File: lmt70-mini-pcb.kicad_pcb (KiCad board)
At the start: 4 copper layers, 7.8 x 8.4 mm, 3 parts, among them P1 CONN_01X04, U1 LMT70

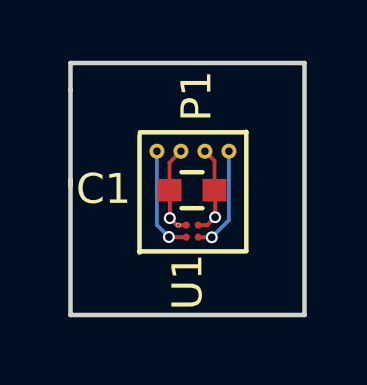
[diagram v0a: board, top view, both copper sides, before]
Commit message: updated pcb to fit bigger cables
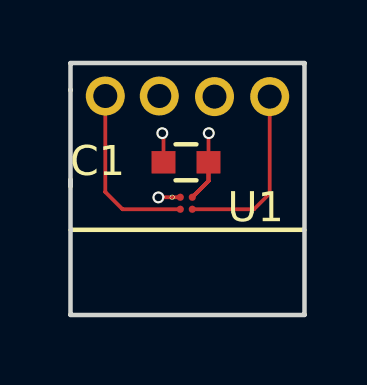
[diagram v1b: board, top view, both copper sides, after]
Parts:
- moved P1 1.94 mm to (150.5, 105.9)
- moved C1 0.95 mm to (151.8, 108.2)
- moved U1 0.95 mm to (151.7, 109.4)
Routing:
- net Net-(P1-Pad4): track 3.56 -> 6.03 mm, vias 1 -> 0
- net Net-(P1-Pad1): track 3.61 -> 5.94 mm, vias 1 -> 0
- net Net-(C1-Pad2): track 5.42 -> 6.46 mm, vias 1 -> 2
- added copper zone on In2.Cu, net Net-(C1-Pad1)
- added copper zone on In1.Cu, net Net-(C1-Pad2)
- removed copper zone on In1.Cu, net Net-(C1-Pad1)
- removed copper zone on In2.Cu, net Net-(C1-Pad2)
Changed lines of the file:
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@@
     (links 6)
     (no_connects 0)
-    (area 146.539667 104.824999 156.460334 113.375001)
+    (area 146.169667 102.996809 156.290001 113.375001)
     (thickness 1.6)
-    (drawings 10)
-    (tracks 28)
+    (drawings 7)
+    (tracks 26)
     (zones 0)
     (modules 3)
@@
     (mod_text_size 1 1)
     (mod_text_width 0.15)
-    (pad_size 1.524 1.524)
-    (pad_drill 0.762)
+    (pad_size 1.3 1.3)
+    (pad_drill 0.8)
     (pad_to_mask_clearance 0.0635)
     (aux_axis_origin 0 0)
@@
   )
   (module Capacitors_SMD:C_0603 (layer F.Cu)
-    (at 152.05 109.14 180)
+    (at 151.85 108.21 180)
     (descr "Capacitor SMD 0603, reflow soldering, AVX (see smccp.pdf)")
     (tags "capacitor 0603")
@@
   )
   (module lmt70:Wire_1x04_mini (layer F.Cu)
-    (at 150.88 107.84)
-    (fp_text reference P1 (at 1.32 -1.84 90) (layer F.SilkS)
+    (at 150.51 105.94)
+    (fp_text reference P1 (at 1.32 -1.84 90) (layer F.SilkS) hide
       (effects (font (size 1 1) (thickness 0.15)))
     )
@@
       (effects (font (size 1 1) (thickness 0.15)))
     )
-    (pad 1 thru_hole circle (at 0 0) (size 0.5 0.5) (drill 0.254) (layers *.Cu *.Mask)
+    (pad 1 thru_hole circle (at -1.35 0.06) (size 1.3 1.3) (drill 0.8) (layers *.Cu *.Mask)
       (net 3 "Net-(P1-Pad1)"))
-    (pad 2 thru_hole circle (at 0.8 0) (size 0.5 0.5) (drill 0.254) (layers *.Cu *.Mask)
+    (pad 2 thru_hole circle (at 0.45 0.06) (size 1.3 1.3) (drill 0.8) (layers *.Cu *.Mask)
       (net 2 "Net-(C1-Pad2)"))
-    (pad 3 thru_hole circle (at 1.6 0) (size 0.5 0.5) (drill 0.254) (layers *.Cu *.Mask)
+    (pad 3 thru_hole circle (at 2.29 0.08) (size 1.3 1.3) (drill 0.8) (layers *.Cu *.Mask)
       (net 1 "Net-(C1-Pad1)"))
-    (pad 4 thru_hole circle (at 2.4 0) (size 0.5 0.5) (drill 0.254) (layers *.Cu *.Mask)
+    (pad 4 thru_hole circle (at 4.13 0.08) (size 1.3 1.3) (drill 0.8) (layers *.Cu *.Mask)
       (net 4 "Net-(P1-Pad4)"))
   )
   (module lmt70:LMT70 (layer F.Cu)
-    (at 151.859524 110.305)
-    (fp_text reference U1 (at 0.040476 1.895 90) (layer F.SilkS)
+    (at 151.659524 109.375)
+    (fp_text reference U1 (at 2.510476 0.335 180) (layer F.SilkS)
       (effects (font (size 1 1) (thickness 0.15)))
     )
@@
   (gr_line (start 148 105.8) (end 148 104.9) (angle 90) (layer Edge.Cuts) (width 0.15))
   (gr_line (start 148 109) (end 148 105.8) (angle 90) (layer Edge.Cuts) (width 0.15))
-  (gr_line (start 153.86 107.21) (end 150.31 107.21) (angle 90) (layer F.SilkS) (width 0.15))
-  (gr_line (start 153.86 111.16) (end 153.86 107.19) (angle 90) (layer F.SilkS) (width 0.15))
-  (gr_line (start 150.3 111.18) (end 153.86 111.18) (angle 90) (layer F.SilkS) (width 0.15))
-  (gr_line (start 150.3 107.31) (end 150.3 111.22) (angle 90) (layer F.SilkS) (width 0.15))
-  (segment (start 152.8 109.14) (end 152.8 108.16) (width 0.127) (layer F.Cu) (net 1))
-  (segment (start 152.8 108.16) (end 152.48 107.84) (width 0.127) (layer F.Cu) (net 1))
-  (segment (start 152.82 110.04) (end 152.82 109.16) (width 0.127) (layer F.Cu) (net 1))
-  (segment (start 152.82 109.16) (end 152.8 109.14) (width 0.127) (layer F.Cu) (net 1))
-  (segment (start 152.555 110.305) (end 152.259524 110.305) (width 0.127) (layer F.Cu) (net 1))
-  (segment (start 152.82 110.04) (end 152.555 110.305) (width 0.127) (layer F.Cu) (net 1))
-  (via (at 152.82 110.04) (size 0.4) (drill 0.254) (layers F.Cu B.Cu) (net 1))
-  (segment (start 152.48 107.84) (end 152.48 109.7) (width 0.127) (layer In2.Cu) (net 1))
-  (segment (start 152.48 109.7) (end 152.82 110.04) (width 0.127) (layer In2.Cu) (net 1))
-  (segment (start 151.31 110.07) (end 151.31 109.15) (width 0.127) (layer F.Cu) (net 2))
-  (segment (start 151.31 109.15) (end 151.3 109.14) (width 0.127) (layer F.Cu) (net 2))
-  (segment (start 151.3 109.14) (end 151.3 108.22) (width 0.127) (layer F.Cu) (net 2))
-  (segment (start 151.3 108.22) (end 151.68 107.84) (width 0.127) (layer F.Cu) (net 2))
-  (segment (start 151.859524 110.305) (end 151.545 110.305) (width 0.127) (layer F.Cu) (net 2))
-  (segment (start 151.68 109.7) (end 151.68 107.84) (width 0.127) (layer In1.Cu) (net 2))
-  (segment (start 151.31 110.07) (end 151.68 109.7) (width 0.127) (layer In1.Cu) (net 2))
-  (via (at 151.31 110.07) (size 0.4) (drill 0.254) (layers F.Cu B.Cu) (net 2))
-  (segment (start 151.545 110.305) (end 151.31 110.07) (width 0.127) (layer F.Cu) (net 2))
-  (segment (start 150.88 110.3) (end 150.88 107.84) (width 0.127) (layer B.Cu) (net 3))
-  (segment (start 151.28 110.7) (end 150.88 110.3) (width 0.127) (layer B.Cu) (net 3))
-  (via (at 151.28 110.7) (size 0.4) (drill 0.254) (layers F.Cu B.Cu) (net 3))
-  (segment (start 151.285 110.705) (end 151.28 110.7) (width 0.127) (layer F.Cu) (net 3))
-  (segment (start 151.859524 110.705) (end 151.285 110.705) (width 0.127) (layer F.Cu) (net 3))
-  (segment (start 152.259524 110.705) (end 152.705 110.705) (width 0.127) (layer F.Cu) (net 4))
-  (segment (start 153.28 110.14) (end 153.28 107.84) (width 0.127) (layer B.Cu) (net 4))
-  (segment (start 152.71 110.71) (end 153.28 110.14) (width 0.127) (layer B.Cu) (net 4))
-  (via (at 152.71 110.71) (size 0.4) (drill 0.254) (layers F.Cu B.Cu) (net 4))
-  (segment (start 152.705 110.705) (end 152.71 110.71) (width 0.127) (layer F.Cu) (net 4))
-  (zone (net 1) (net_name "Net-(C1-Pad1)") (layer In1.Cu) (hatch edge 0.508)
+  (gr_line (start 148 110.46) (end 155.8 110.46) (angle 90) (layer F.SilkS) (width 0.15))
+  (segment (start 152.6 108.21) (end 152.6 108.834524) (width 0.127) (layer F.Cu) (net 1))
+  (segment (start 152.6 108.834524) (end 152.059524 109.375) (width 0.127) (layer F.Cu) (net 1))
+  (segment (start 152.8 106.02) (end 152.8 107.05) (width 0.127) (layer In2.Cu) (net 1))
+  (segment (start 152.8 107.05) (end 152.61 107.24) (width 0.127) (layer In2.Cu) (net 1))
+  (via (at 152.61 107.24) (size 0.4) (drill 0.254) (layers F.Cu B.Cu) (net 1))
+  (segment (start 152.61 107.24) (end 152.6 107.25) (width 0.127) (layer F.Cu) (net 1))
+  (segment (start 152.6 107.25) (end 152.6 108.834524) (width 0.127) (layer F.Cu) (net 1))
+  (segment (start 152.6 108.834524) (end 152.059524 109.375) (width 0.127) (layer F.Cu) (net 1))
+  (segment (start 152.62 108.23) (end 152.6 108.21) (width 0.127) (layer F.Cu) (net 1))
+  (segment (start 151.659524 109.375) (end 150.935 109.375) (width 0.127) (layer F.Cu) (net 2))
+  (segment (start 150.79 109.24) (end 150.96 106) (width 0.127) (layer In1.Cu) (net 2))
+  (segment (start 150.93 109.38) (end 150.79 109.24) (width 0.127) (layer In1.Cu) (net 2))
+  (via (at 150.93 109.38) (size 0.4) (drill 0.254) (layers F.Cu B.Cu) (net 2))
+  (segment (start 150.935 109.375) (end 150.93 109.38) (width 0.127) (layer F.Cu) (net 2))
+  (segment (start 150.96 106) (end 150.96 107.14) (width 0.127) (layer In1.Cu) (net 2))
+  (segment (start 151.1 107.28) (end 151.1 108.21) (width 0.127) (layer F.Cu) (net 2))
+  (segment (start 151.06 107.24) (end 151.1 107.28) (width 0.127) (layer F.Cu) (net 2))
+  (via (at 151.06 107.24) (size 0.4) (drill 0.254) (layers F.Cu B.Cu) (net 2))
+  (segment (start 150.96 107.14) (end 151.06 107.24) (width 0.127) (layer In1.Cu) (net 2))
+  (segment (start 151.11 108.22) (end 151.1 108.21) (width 0.127) (layer F.Cu) (net 2))
+  (segment (start 151.659524 109.775) (end 149.735 109.775) (width 0.127) (layer F.Cu) (net 3))
+  (segment (start 149.16 109.2) (end 149.16 106) (width 0.127) (layer F.Cu) (net 3))
+  (segment (start 149.735 109.775) (end 149.16 109.2) (width 0.127) (layer F.Cu) (net 3))
+  (segment (start 152.059524 109.775) (end 154.115 109.775) (width 0.127) (layer F.Cu) (net 4))
+  (segment (start 154.64 109.25) (end 154.64 106.02) (width 0.127) (layer F.Cu) (net 4))
+  (segment (start 154.115 109.775) (end 154.64 109.25) (width 0.127) (layer F.Cu) (net 4))
+  (zone (net 1) (net_name "Net-(C1-Pad1)") (layer In2.Cu) (hatch edge 0.508)
     (connect_pads (clearance 0.127))
     (min_thickness 0.127)
@@
     (polygon
       (pts
-        (xy 153.9 111.2) (xy 150.35 111.28) (xy 150.37 107.2) (xy 153.98 107.13)
+        (xy 155.86 104.83) (xy 155.859964 104.84) (xy 155.86 104.84) (xy 155.85 110.38) (xy 155.840036 110.38)
+        (xy 155.84 110.39) (xy 147.97 110.39) (xy 147.969982 110.38) (xy 147.95 110.38) (xy 147.92 104.82)
+        (xy 147.96 104.820101) (xy 147.96 104.82)
       )
     )
   )
-  (zone (net 2) (net_name "Net-(C1-Pad2)") (layer In2.Cu) (hatch edge 0.508)
+  (zone (net 2) (net_name "Net-(C1-Pad2)") (layer In1.Cu) (hatch edge 0.508)
     (connect_pads (clearance 0.127))
     (min_thickness 0.127)
@@
     (polygon
       (pts
-        (xy 153.94 111.27) (xy 150.27 111.27) (xy 150.27 107.246233) (xy 153.91 107.06)
+        (xy 147.72 104.49) (xy 147.69 110.47) (xy 156.29 110.46) (xy 156.29 104.58)
       )
     )

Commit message: termo buffer from cable
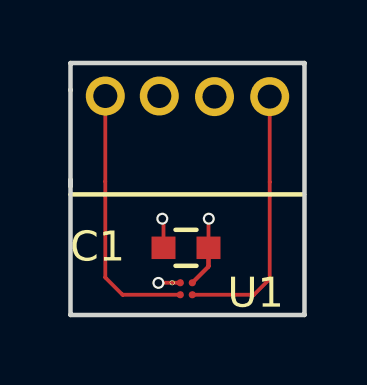
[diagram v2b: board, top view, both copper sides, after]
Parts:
- moved C1 2.85 mm to (151.8, 111.1)
- moved U1 2.85 mm to (151.7, 112.2)
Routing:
- net Net-(C1-Pad2): track 6.46 -> 9.37 mm
- net Net-(P1-Pad4): track 6.03 -> 8.88 mm
- net Net-(P1-Pad1): track 5.94 -> 8.79 mm
- net Net-(C1-Pad1): track 5.08 -> 7.93 mm
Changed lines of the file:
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@@
     (thickness 1.6)
     (drawings 7)
-    (tracks 26)
+    (tracks 32)
     (zones 0)
     (modules 3)
@@
   )
   (module Capacitors_SMD:C_0603 (layer F.Cu)
-    (at 151.85 108.21 180)
+    (at 151.85 111.06 180)
     (descr "Capacitor SMD 0603, reflow soldering, AVX (see smccp.pdf)")
     (tags "capacitor 0603")
@@
   )
   (module lmt70:LMT70 (layer F.Cu)
-    (at 151.659524 109.375)
+    (at 151.659524 112.225)
     (fp_text reference U1 (at 2.510476 0.335 180) (layer F.SilkS)
       (effects (font (size 1 1) (thickness 0.15)))
@@
   (gr_line (start 148 105.8) (end 148 104.9) (angle 90) (layer Edge.Cuts) (width 0.15))
   (gr_line (start 148 109) (end 148 105.8) (angle 90) (layer Edge.Cuts) (width 0.15))
-  (gr_line (start 148 110.46) (end 155.8 110.46) (angle 90) (layer F.SilkS) (width 0.15))
-  (segment (start 152.6 108.21) (end 152.6 108.834524) (width 0.127) (layer F.Cu) (net 1))
-  (segment (start 152.6 108.834524) (end 152.059524 109.375) (width 0.127) (layer F.Cu) (net 1))
-  (segment (start 152.8 106.02) (end 152.8 107.05) (width 0.127) (layer In2.Cu) (net 1))
-  (segment (start 152.8 107.05) (end 152.61 107.24) (width 0.127) (layer In2.Cu) (net 1))
-  (via (at 152.61 107.24) (size 0.4) (drill 0.254) (layers F.Cu B.Cu) (net 1))
-  (segment (start 152.61 107.24) (end 152.6 107.25) (width 0.127) (layer F.Cu) (net 1))
-  (segment (start 152.6 107.25) (end 152.6 108.834524) (width 0.127) (layer F.Cu) (net 1))
-  (segment (start 152.6 108.834524) (end 152.059524 109.375) (width 0.127) (layer F.Cu) (net 1))
-  (segment (start 152.62 108.23) (end 152.6 108.21) (width 0.127) (layer F.Cu) (net 1))
-  (segment (start 151.659524 109.375) (end 150.935 109.375) (width 0.127) (layer F.Cu) (net 2))
-  (segment (start 150.79 109.24) (end 150.96 106) (width 0.127) (layer In1.Cu) (net 2))
-  (segment (start 150.93 109.38) (end 150.79 109.24) (width 0.127) (layer In1.Cu) (net 2))
-  (via (at 150.93 109.38) (size 0.4) (drill 0.254) (layers F.Cu B.Cu) (net 2))
-  (segment (start 150.935 109.375) (end 150.93 109.38) (width 0.127) (layer F.Cu) (net 2))
-  (segment (start 150.96 106) (end 150.96 107.14) (width 0.127) (layer In1.Cu) (net 2))
-  (segment (start 151.1 107.28) (end 151.1 108.21) (width 0.127) (layer F.Cu) (net 2))
-  (segment (start 151.06 107.24) (end 151.1 107.28) (width 0.127) (layer F.Cu) (net 2))
-  (via (at 151.06 107.24) (size 0.4) (drill 0.254) (layers F.Cu B.Cu) (net 2))
-  (segment (start 150.96 107.14) (end 151.06 107.24) (width 0.127) (layer In1.Cu) (net 2))
-  (segment (start 151.11 108.22) (end 151.1 108.21) (width 0.127) (layer F.Cu) (net 2))
-  (segment (start 151.659524 109.775) (end 149.735 109.775) (width 0.127) (layer F.Cu) (net 3))
-  (segment (start 149.16 109.2) (end 149.16 106) (width 0.127) (layer F.Cu) (net 3))
-  (segment (start 149.735 109.775) (end 149.16 109.2) (width 0.127) (layer F.Cu) (net 3))
-  (segment (start 152.059524 109.775) (end 154.115 109.775) (width 0.127) (layer F.Cu) (net 4))
-  (segment (start 154.64 109.25) (end 154.64 106.02) (width 0.127) (layer F.Cu) (net 4))
-  (segment (start 154.115 109.775) (end 154.64 109.25) (width 0.127) (layer F.Cu) (net 4))
+  (gr_line (start 147.99 109.28) (end 155.79 109.28) (angle 90) (layer F.SilkS) (width 0.15))
+  (segment (start 152.8 106.02) (end 152.8 108.87) (width 0.127) (layer In2.Cu) (net 1))
+  (segment (start 152.6 110.1) (end 152.6 111.684524) (width 0.127) (layer F.Cu) (net 1))
+  (segment (start 152.61 110.09) (end 152.6 110.1) (width 0.127) (layer F.Cu) (net 1))
+  (via (at 152.61 110.09) (size 0.4) (drill 0.254) (layers F.Cu B.Cu) (net 1))
+  (segment (start 152.8 109.9) (end 152.61 110.09) (width 0.127) (layer In2.Cu) (net 1))
+  (segment (start 152.8 108.87) (end 152.8 109.9) (width 0.127) (layer In2.Cu) (net 1))
+  (segment (start 152.6 111.06) (end 152.6 111.684524) (width 0.127) (layer F.Cu) (net 1))
+  (segment (start 152.6 111.684524) (end 152.059524 112.225) (width 0.127) (layer F.Cu) (net 1))
+  (segment (start 152.6 111.684524) (end 152.059524 112.225) (width 0.127) (layer F.Cu) (net 1))
+  (segment (start 152.62 111.08) (end 152.6 111.06) (width 0.127) (layer F.Cu) (net 1))
+  (segment (start 150.956833 108.910359) (end 150.956833 106.003167) (width 0.127) (layer In1.Cu) (net 2))
+  (segment (start 150.956833 106.003167) (end 150.96 106) (width 0.127) (layer In1.Cu) (net 2))
+  (segment (start 151.659524 112.225) (end 150.935 112.225) (width 0.127) (layer F.Cu) (net 2))
+  (segment (start 150.79 112.09) (end 150.956833 108.910359) (width 0.127) (layer In1.Cu) (net 2))
+  (segment (start 150.956833 108.910359) (end 150.96 108.85) (width 0.127) (layer In1.Cu) (net 2))
+  (segment (start 150.93 112.23) (end 150.79 112.09) (width 0.127) (layer In1.Cu) (net 2))
+  (via (at 150.93 112.23) (size 0.4) (drill 0.254) (layers F.Cu B.Cu) (net 2))
+  (segment (start 150.935 112.225) (end 150.93 112.23) (width 0.127) (layer F.Cu) (net 2))
+  (segment (start 150.96 108.85) (end 150.96 109.99) (width 0.127) (layer In1.Cu) (net 2))
+  (segment (start 151.1 110.13) (end 151.1 111.06) (width 0.127) (layer F.Cu) (net 2))
+  (segment (start 151.06 110.09) (end 151.1 110.13) (width 0.127) (layer F.Cu) (net 2))
+  (via (at 151.06 110.09) (size 0.4) (drill 0.254) (layers F.Cu B.Cu) (net 2))
+  (segment (start 150.96 109.99) (end 151.06 110.09) (width 0.127) (layer In1.Cu) (net 2))
+  (segment (start 151.11 111.07) (end 151.1 111.06) (width 0.127) (layer F.Cu) (net 2))
+  (segment (start 149.16 106) (end 149.16 108.85) (width 0.127) (layer F.Cu) (net 3))
+  (segment (start 149.735 112.625) (end 149.16 112.05) (width 0.127) (layer F.Cu) (net 3))
+  (segment (start 149.16 112.05) (end 149.16 108.85) (width 0.127) (layer F.Cu) (net 3))
+  (segment (start 149.735 112.625) (end 151.659524 112.625) (width 0.127) (layer F.Cu) (net 3))
+  (segment (start 154.64 106.02) (end 154.64 108.87) (width 0.127) (layer F.Cu) (net 4))
+  (segment (start 154.115 112.625) (end 154.64 112.1) (width 0.127) (layer F.Cu) (net 4))
+  (segment (start 154.64 112.1) (end 154.64 108.87) (width 0.127) (layer F.Cu) (net 4))
+  (segment (start 154.115 112.625) (end 152.059524 112.625) (width 0.127) (layer F.Cu) (net 4))
   (zone (net 1) (net_name "Net-(C1-Pad1)") (layer In2.Cu) (hatch edge 0.508)
     (connect_pads (clearance 0.127))
@@
     (polygon
       (pts
-        (xy 155.86 104.83) (xy 155.859964 104.84) (xy 155.86 104.84) (xy 155.85 110.38) (xy 155.840036 110.38)
-        (xy 155.84 110.39) (xy 147.97 110.39) (xy 147.969982 110.38) (xy 147.95 110.38) (xy 147.92 104.82)
-        (xy 147.96 104.820101) (xy 147.96 104.82)
+        (xy 155.82 109.27) (xy 155.859964 107.69) (xy 155.86 107.69) (xy 155.85 113.23) (xy 155.840036 113.23)
+        (xy 155.84 113.24) (xy 147.97 113.24) (xy 147.969982 113.23) (xy 147.95 113.23) (xy 147.9301 109.260013)
       )
     )
@@
     (polygon
       (pts
-        (xy 147.72 104.49) (xy 147.69 110.47) (xy 156.29 110.46) (xy 156.29 104.58)
+        (xy 147.64 109.19) (xy 147.69 113.32) (xy 156.29 113.31) (xy 156.21 109.28)
       )
     )
+  )
+  (zone (net 1) (net_name "Net-(C1-Pad1)") (layer In2.Cu) (hatch edge 0.508)
+    (connect_pads (clearance 0.127))
+    (min_thickness 0.254)
+    (fill yes (arc_segments 16) (thermal_gap 0.508) (thermal_bridge_width 0.508))
+    (polygon
+      (pts
+        (xy 147.92 109.26) (xy 147.96 107.670101) (xy 147.93 109.24) (xy 147.9301 109.260013)
+      )
+    )
